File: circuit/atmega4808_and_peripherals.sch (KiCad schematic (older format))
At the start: 24 parts, among them Q1 BSS138, U10 ATmega4808-X, U7 SN65HVD72, U8 TC4424AVOA, U9 MCP9700A

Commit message: Update schematic to rev0.2
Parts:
- added J3: Conn_02x03_Odd_Even, symbol Connector_Generic:Conn_02x03_Odd_Even
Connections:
- net labels added: RESET, RX0_to_ESP, TX0_to_ESP, UDPI
- wire segments 121 -> 131
- no-connect marks 1 -> 4
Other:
- note added: "UDPI Programming Interface\n"
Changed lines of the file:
@@
 Title ""
 Date "2020-04-10"
-Rev "0.1"
+Rev "0.2"
 Comp ""
 Comment1 "TODO: ESP32 circuit"
-Comment2 "TODO: Serial comms and programming interface"
-Comment3 ""
+Comment2 "TODO: Serial comms interface"
+Comment3 "DONE: UDPI Interface"
 Comment4 ""
 $EndDescr
@@
 Wire Wire Line
 	5150 4700 5000 4700
-Text HLabel 5000 4400 0    50   Output ~ 0
+Text HLabel 5000 4400 0    50   Input ~ 0
 CT0
-Text HLabel 5000 4550 0    50   Output ~ 0
+Text HLabel 5000 4550 0    50   Input ~ 0
 CT1
-Text HLabel 5000 4700 0    50   Output ~ 0
+Text HLabel 5000 4700 0    50   Input ~ 0
 CT2
 Wire Wire Line
@@
 Text HLabel 6900 3200 2    50   Output ~ 0
 Reed_Relay
+$Comp
+L Connector_Generic:Conn_02x03_Odd_Even J3
+U 1 1 5E9E428D
+P 8450 1850
+F 0 "J3" H 8500 2167 50  0000 C CNN
+F 1 "Conn_02x03_Odd_Even" H 8500 2076 50  0000 C CNN
+F 2 "" H 8450 1850 50  0001 C CNN
+F 3 "~" H 8450 1850 50  0001 C CNN
+	1    8450 1850
+	1    0    0    -1
+$EndComp
+Wire Wire Line
+	6350 4250 7900 4250
+Wire Wire Line
+	7900 4250 7900 1750
+Wire Wire Line
+	7900 1750 8250 1750
+Text Label 8150 1750 2    50   ~ 0
+UDPI
+Wire Wire Line
+	8750 1750 9000 1750
+Wire Wire Line
+	9000 1750 9000 1500
+$Comp
+L power:+3.3V #PWR030
+U 1 1 5E9F3B24
+P 9000 1500
+F 0 "#PWR030" H 9000 1350 50  0001 C CNN
+F 1 "+3.3V" H 9015 1673 50  0000 C CNN
+F 2 "" H 9000 1500 50  0001 C CNN
+F 3 "" H 9000 1500 50  0001 C CNN
+	1    9000 1500
+	1    0    0    -1
+$EndComp
+Wire Wire Line
+	8750 1950 9000 1950
+Wire Wire Line
+	9000 1950 9000 2150
+$Comp
+L power:GND #PWR031
+U 1 1 5E9F8F1C
+P 9000 2150
+F 0 "#PWR031" H 9000 1900 50  0001 C CNN
+F 1 "GND" H 9005 1977 50  0000 C CNN
+F 2 "" H 9000 2150 50  0001 C CNN
+F 3 "" H 9000 2150 50  0001 C CNN
+	1    9000 2150
+	1    0    0    -1
+$EndComp
+NoConn ~ 8750 1850
+NoConn ~ 8250 1850
+NoConn ~ 8250 1950
+Wire Notes Line
+	7750 1050 7750 2450
+Wire Notes Line
+	7750 2450 9350 2450
+Wire Notes Line
+	9350 2450 9350 1050
+Wire Notes Line
+	9350 1050 7750 1050
+Text Notes 9100 1150 2    50   ~ 0
+UDPI Programming Interface\n
+Wire Wire Line
+	6350 3500 6900 3500
+Wire Wire Line
+	6350 3650 6900 3650
+Wire Wire Line
+	6350 4400 6900 4400
+Text Label 6900 4400 2    50   ~ 0
+RESET
+Text Label 6900 3500 2    50   ~ 0
+RX0_to_ESP
+Text Label 6900 3650 2    50   ~ 0
+TX0_to_ESP
 $EndSCHEMATC

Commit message: Update Schematic with Prof. Moor's suggestions
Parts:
- removed J3: Conn_02x03_Odd_Even, symbol Connector_Generic:Conn_02x03_Odd_Even
- added J? (x2): Conn_02x04_Top_Bottom, symbol Connector_Generic:Conn_02x04_Top_Bottom
- added U?: ESP32-WROOM-32, RF_Module:ESP32-WROOM-32, symbol RF_Module:ESP32-WROOM-32
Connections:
- net labels added: ATmega_RESET, ATmega_RX0, ATmega_TX0, ATmega_UDPI, EN, ESP_IO12, ESP_RX0, ESP_RX2, ESP_TX0, ESP_TX2, ESP_VDD, IO0, IO2
- net labels removed: RESET, RX0_to_ESP, TX0_to_ESP, UDPI
- wire segments 131 -> 162
- no-connect marks 4 -> 1
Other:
- note added: "ATmega/ESP Programming & Serial Comms\n"
- note removed: "UDPI Programming Interface\n"

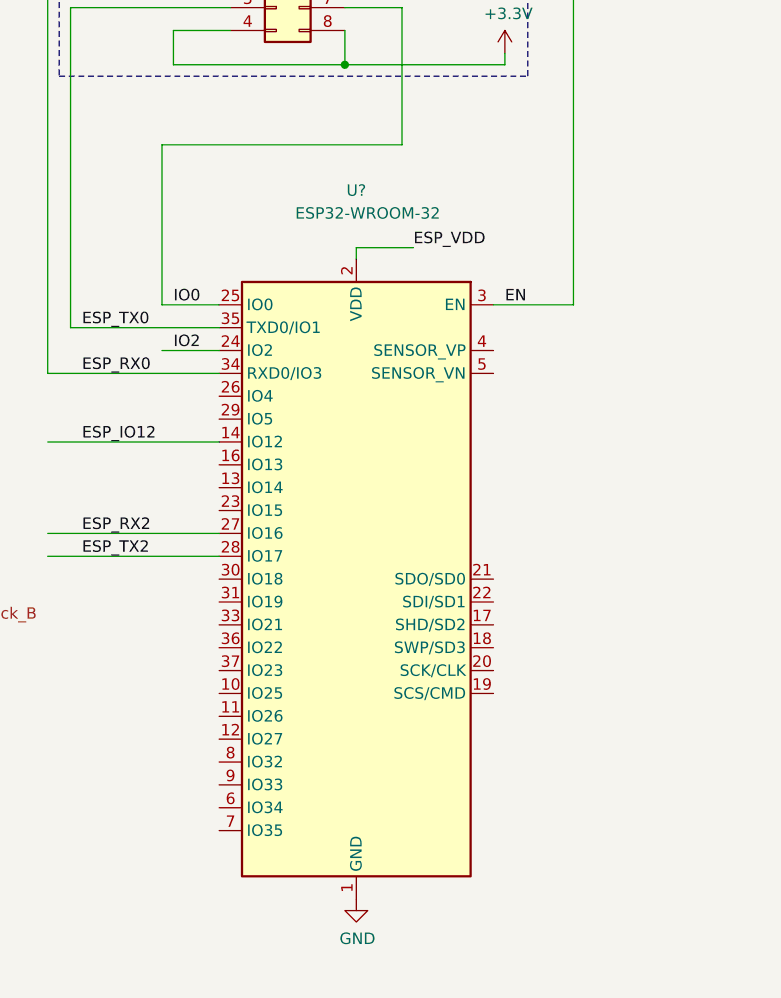
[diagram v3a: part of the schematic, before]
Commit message: Update schematic with suggestions
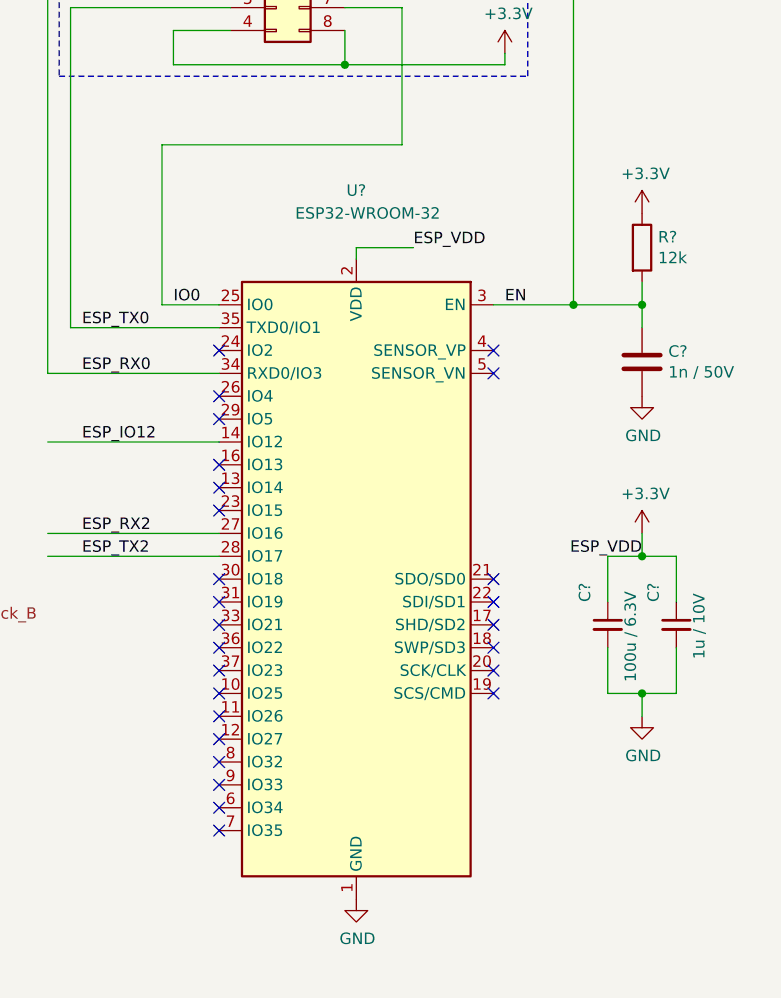
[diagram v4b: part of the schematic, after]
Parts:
- added C?: 1n / 50V, symbol Device:C
- added C?: 100u / 6.3V, symbol Device:C_Small
- added C?: 1u / 10V, symbol Device:C_Small
- added R?: 12k, symbol Device:R
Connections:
- net labels removed: IO2
- wire segments 162 -> 174
- no-connect marks 1 -> 27
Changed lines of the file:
@@
 Text Label 10200 3200 0    50   ~ 0
 EN
-Wire Wire Line
-	8950 3400 8700 3400
-Text Label 8750 3400 0    50   ~ 0
-IO2
 Text Label 9800 2950 0    50   ~ 0
 ESP_VDD
@@
 Wire Wire Line
 	9800 2950 9550 2950
+$Comp
+L Device:R R?
+U 1 1 5EBDA7D4
+P 10800 2950
+F 0 "R?" H 10870 2996 50  0000 L CNN
+F 1 "12k" H 10870 2905 50  0000 L CNN
+F 2 "" V 10730 2950 50  0001 C CNN
+F 3 "~" H 10800 2950 50  0001 C CNN
+	1    10800 2950
+	1    0    0    -1
+$EndComp
+$Comp
+L Device:C C?
+U 1 1 5EBDAC66
+P 10800 3450
+F 0 "C?" H 10915 3496 50  0000 L CNN
+F 1 "1n / 50V" H 10915 3405 50  0000 L CNN
+F 2 "" H 10838 3300 50  0001 C CNN
+F 3 "~" H 10800 3450 50  0001 C CNN
+	1    10800 3450
+	1    0    0    -1
+$EndComp
+$Comp
+L power:GND #PWR?
+U 1 1 5EBDB705
+P 10800 3600
+F 0 "#PWR?" H 10800 3350 50  0001 C CNN
+F 1 "GND" H 10805 3427 50  0000 C CNN
+F 2 "" H 10800 3600 50  0001 C CNN
+F 3 "" H 10800 3600 50  0001 C CNN
+	1    10800 3600
+	1    0    0    -1
+$EndComp
+$Comp
+L power:+3.3V #PWR?
+U 1 1 5EBDC16A
+P 10800 2800
+F 0 "#PWR?" H 10800 2650 50  0001 C CNN
+F 1 "+3.3V" H 10815 2973 50  0000 C CNN
+F 2 "" H 10800 2800 50  0001 C CNN
+F 3 "" H 10800 2800 50  0001 C CNN
+	1    10800 2800
+	1    0    0    -1
+$EndComp
+Wire Wire Line
+	10800 3100 10800 3200
+Wire Wire Line
+	10800 3200 10500 3200
+Connection ~ 10800 3200
+Wire Wire Line
+	10800 3200 10800 3300
+Connection ~ 10500 3200
+$Comp
+L Device:C_Small C?
+U 1 1 5EC15E77
+P 10650 4600
+F 0 "C?" V 10550 4700 50  0000 L CNN
+F 1 "100u / 6.3V" V 10750 4350 50  0000 L CNN
+F 2 "" H 10650 4600 50  0001 C CNN
+F 3 "~" H 10650 4600 50  0001 C CNN
+	1    10650 4600
+	1    0    0    -1
+$EndComp
+$Comp
+L Device:C_Small C?
+U 1 1 5EC16D76
+P 10950 4600
+F 0 "C?" V 10850 4700 50  0000 L CNN
+F 1 "1u / 10V" V 11050 4450 50  0000 L CNN
+F 2 "" H 10950 4600 50  0001 C CNN
+F 3 "~" H 10950 4600 50  0001 C CNN
+	1    10950 4600
+	1    0    0    -1
+$EndComp
+Wire Wire Line
+	10650 4700 10650 4900
+Wire Wire Line
+	10650 4900 10800 4900
+Wire Wire Line
+	10950 4900 10950 4700
+Wire Wire Line
+	10800 4900 10800 5000
+Connection ~ 10800 4900
+Wire Wire Line
+	10800 4900 10950 4900
+$Comp
+L power:GND #PWR?
+U 1 1 5EC27338
+P 10800 5000
+F 0 "#PWR?" H 10800 4750 50  0001 C CNN
+F 1 "GND" H 10805 4827 50  0000 C CNN
+F 2 "" H 10800 5000 50  0001 C CNN
+F 3 "" H 10800 5000 50  0001 C CNN
+	1    10800 5000
+	1    0    0    -1
+$EndComp
+Wire Wire Line
+	10650 4500 10650 4300
+Wire Wire Line
+	10650 4300 10800 4300
+Wire Wire Line
+	10950 4300 10950 4500
+Wire Wire Line
+	10800 4300 10800 4200
+Connection ~ 10800 4300
+Wire Wire Line
+	10800 4300 10950 4300
+$Comp
+L power:+3.3V #PWR?
+U 1 1 5EC38273
+P 10800 4200
+F 0 "#PWR?" H 10800 4050 50  0001 C CNN
+F 1 "+3.3V" H 10815 4373 50  0000 C CNN
+F 2 "" H 10800 4200 50  0001 C CNN
+F 3 "" H 10800 4200 50  0001 C CNN
+	1    10800 4200
+	1    0    0    -1
+$EndComp
+Text Label 10800 4300 2    50   ~ 0
+ESP_VDD
+NoConn ~ 8950 3600
+NoConn ~ 8950 3700
+NoConn ~ 8950 3900
+NoConn ~ 8950 4000
+NoConn ~ 8950 4100
+NoConn ~ 8950 4400
+NoConn ~ 8950 4500
+NoConn ~ 8950 4600
+NoConn ~ 8950 4700
+NoConn ~ 8950 4800
+NoConn ~ 8950 4900
+NoConn ~ 8950 5000
+NoConn ~ 8950 5100
+NoConn ~ 8950 5200
+NoConn ~ 8950 5300
+NoConn ~ 8950 5400
+NoConn ~ 8950 5500
+NoConn ~ 10150 4900
+NoConn ~ 10150 4800
+NoConn ~ 10150 4700
+NoConn ~ 10150 4600
+NoConn ~ 10150 4500
+NoConn ~ 10150 4400
+NoConn ~ 10150 3400
+NoConn ~ 10150 3500
+NoConn ~ 8950 3400
 $EndSCHEMATC

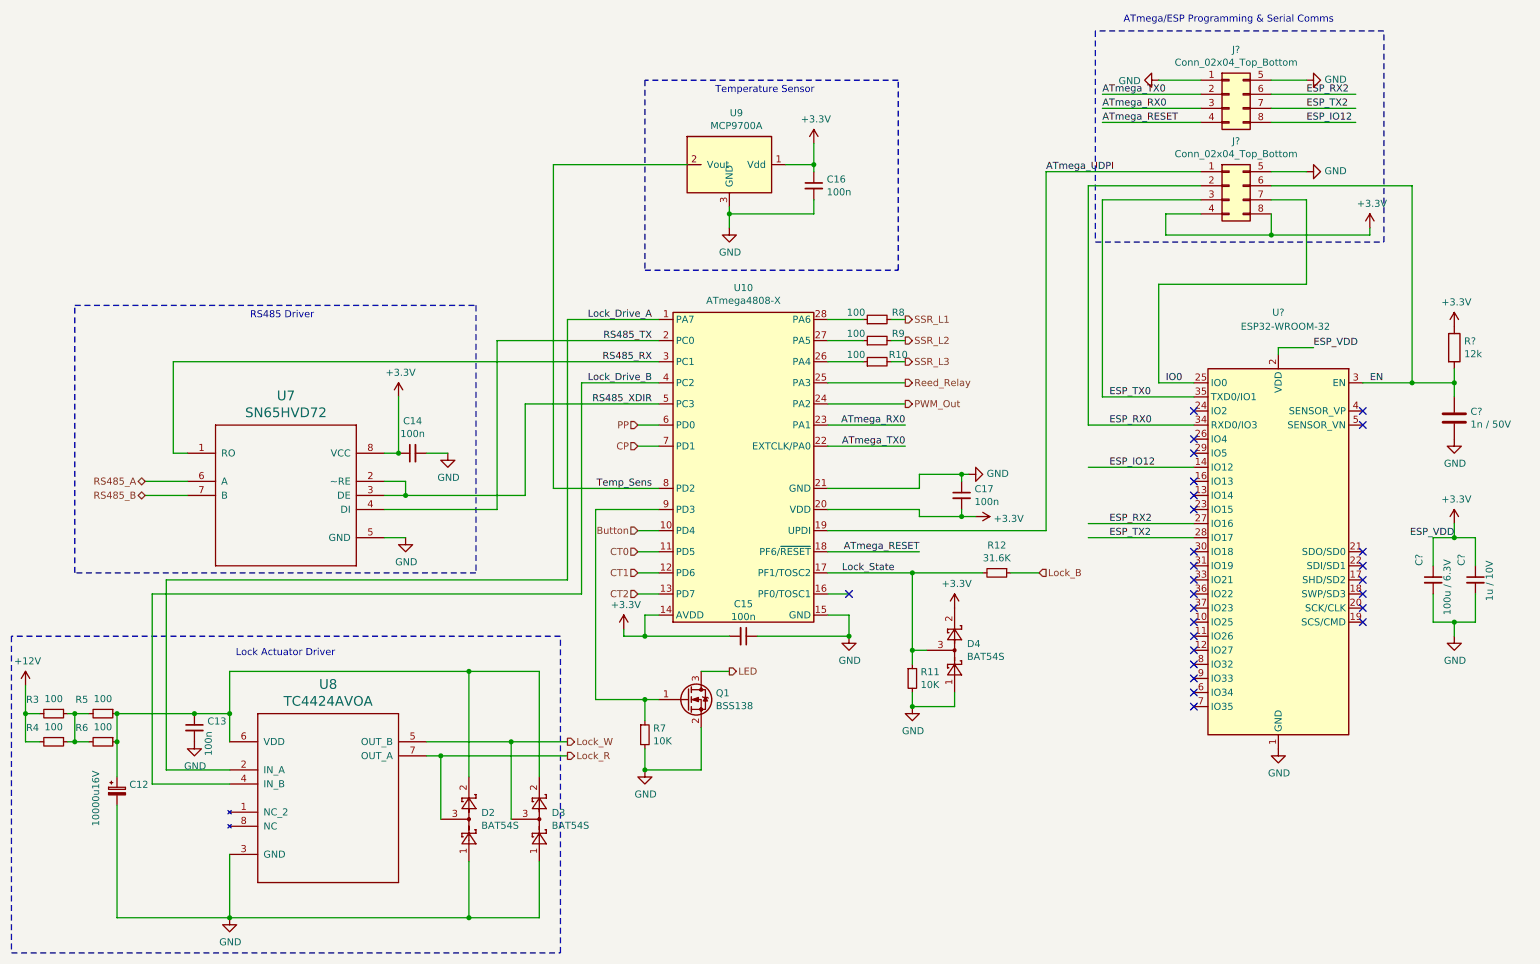
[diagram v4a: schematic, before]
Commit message: Edit schematic to rev0.6
Updated schematic with ESP32, CT inputs moved, Button input circuit new.
Temp sens removed, will use internal sensor in ATmega4808
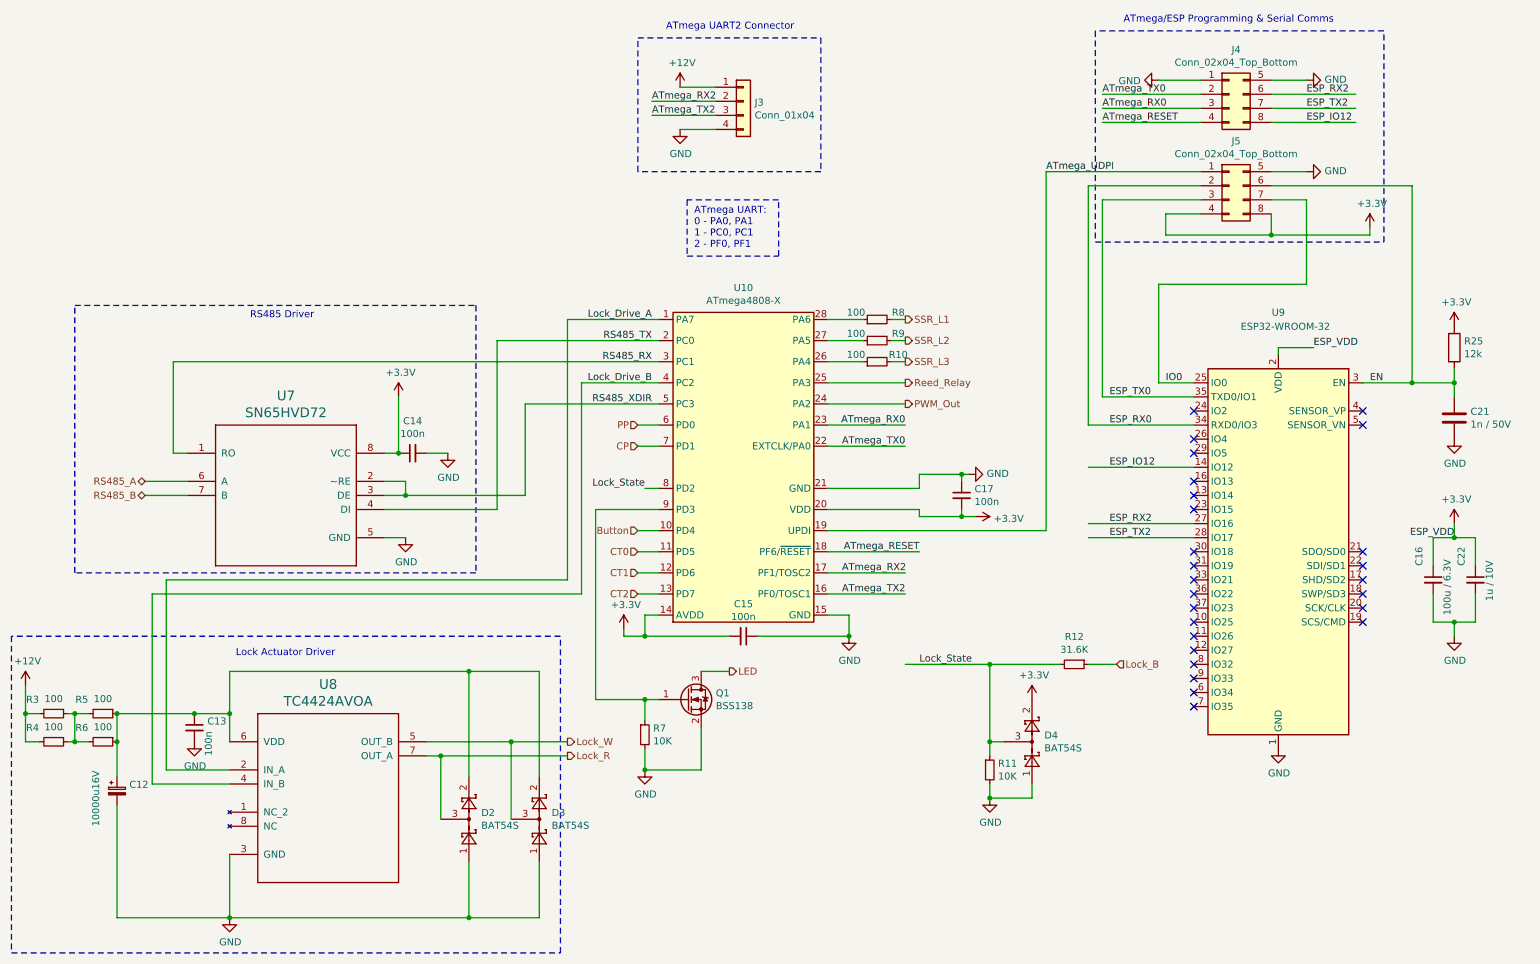
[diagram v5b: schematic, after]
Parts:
- removed C16: 100n, symbol Device:C_Small
- removed U9: MCP9700A, symbol smartevse:MCP9700A
- added J3: Conn_01x04, symbol Connector_Generic:Conn_01x04
- gave numbers to parts that had none: 7
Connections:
- net labels added: ATmega_RX2, ATmega_TX2
- net labels removed: Temp_Sens
- wire segments 174 -> 170
- no-connect marks 27 -> 26
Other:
- note added: "ATmega UART2 Connector\n"
- note added: "ATmega UART:\n0 - PA0, PA1\n1 - PC0, PC1\n2 - PF0, PF1"
- note removed: "Temperature Sensor\n"
- moved on the sheet: D4, R11, R12

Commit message: Update schematic
Schematic updated with latest changes and preparation for footprint assignment
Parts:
- J3: footprint (none) -> Connector_PinHeader_2.54mm:PinHeader_1x04_P2.54mm_Vertical
- J4, J5: footprint (none) -> Connector_PinHeader_2.54mm:PinHeader_2x04_P2.54mm_Vertical
- Q1: footprint Package_TO_SOT_SMD:SOT-23 -> (none)
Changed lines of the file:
@@
 F 0 "Q1" H 5554 5496 50  0000 L CNN
 F 1 "BSS138" H 5554 5405 50  0000 L CNN
-F 2 "Package_TO_SOT_SMD:SOT-23" H 5550 5375 50  0001 L CIN
+F 2 "" H 5550 5375 50  0001 L CIN
 F 3 "https://www.fairchildsemi.com/datasheets/BS/BSS138.pdf" H 5350 5450 50  0001 L CNN
 	1    5350 5450
@@
 F 0 "J4" H 9250 1467 50  0000 C CNN
 F 1 "Conn_02x04_Top_Bottom" H 9250 1376 50  0000 C CNN
-F 2 "" H 9200 1150 50  0001 C CNN
+F 2 "Connector_PinHeader_2.54mm:PinHeader_2x04_P2.54mm_Vertical" H 9200 1150 50  0001 C CNN
 F 3 "~" H 9200 1150 50  0001 C CNN
 	1    9200 1150
@@
 F 0 "J5" H 9250 2117 50  0000 C CNN
 F 1 "Conn_02x04_Top_Bottom" H 9250 2026 50  0000 C CNN
-F 2 "" H 9200 1800 50  0001 C CNN
+F 2 "Connector_PinHeader_2.54mm:PinHeader_2x04_P2.54mm_Vertical" H 9200 1800 50  0001 C CNN
 F 3 "~" H 9200 1800 50  0001 C CNN
 	1    9200 1800
@@
 F 0 "J3" H 5830 1192 50  0000 L CNN
 F 1 "Conn_01x04" H 5830 1101 50  0000 L CNN
-F 2 "" H 5750 1200 50  0001 C CNN
+F 2 "Connector_PinHeader_2.54mm:PinHeader_1x04_P2.54mm_Vertical" H 5750 1200 50  0001 C CNN
 F 3 "~" H 5750 1200 50  0001 C CNN
 	1    5750 1200
